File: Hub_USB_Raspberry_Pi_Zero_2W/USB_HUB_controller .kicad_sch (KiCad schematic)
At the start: 1 part, among them U3 CH334F

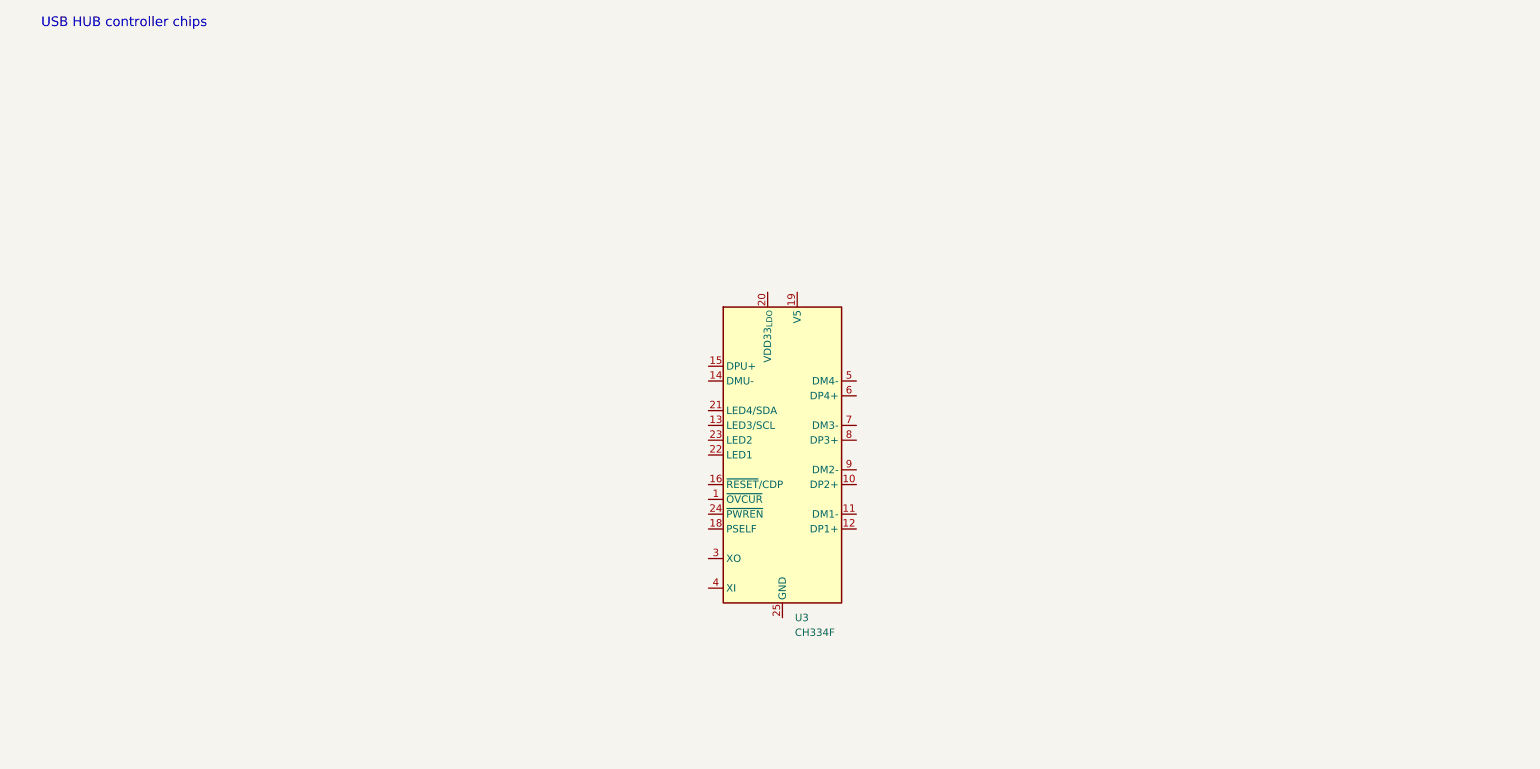
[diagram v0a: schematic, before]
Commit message: Update kicad HUB
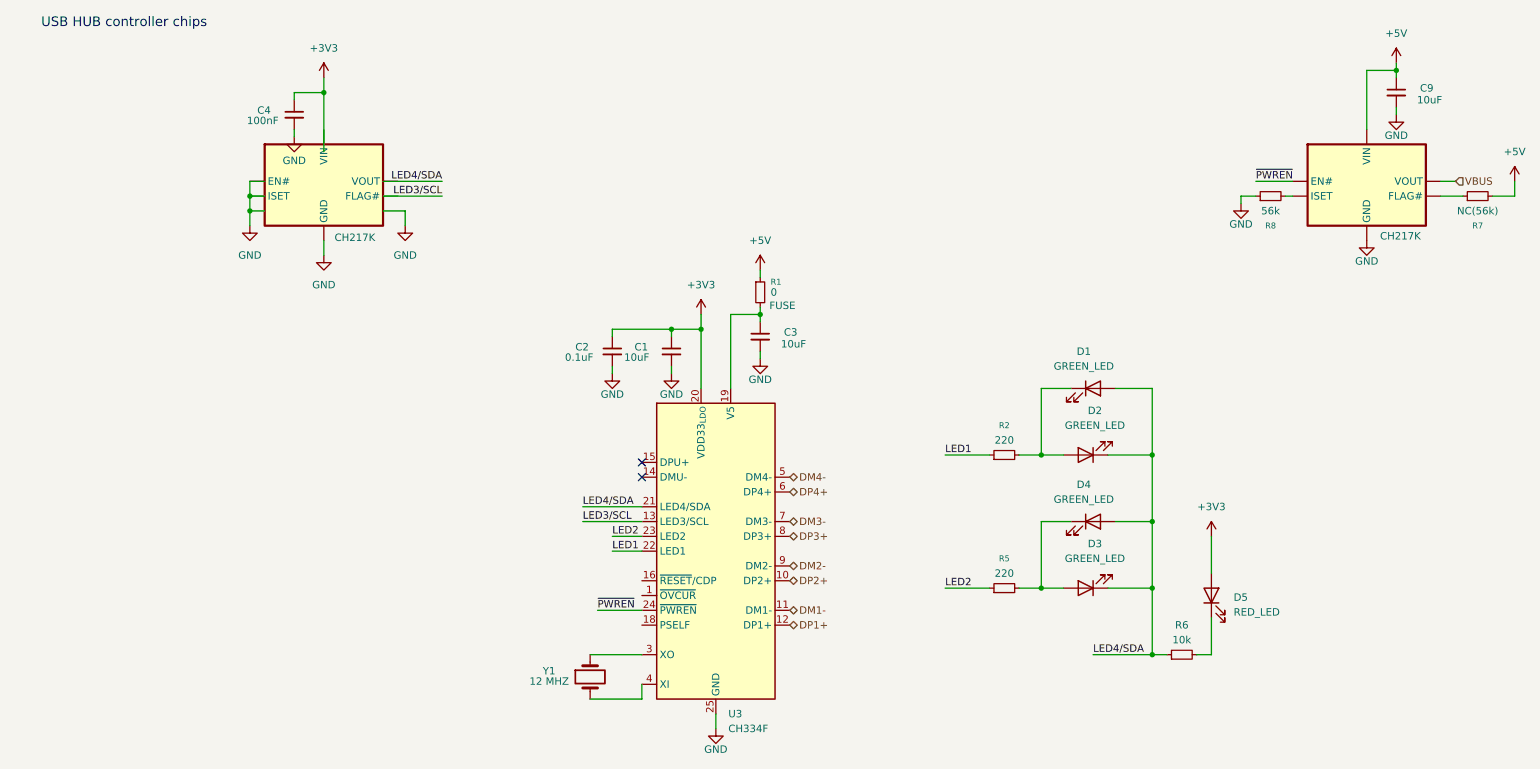
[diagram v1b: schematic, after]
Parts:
- added C1, C3, C9: 10uF, Capacitor_SMD:C_0603_1608Metric, symbol Device:C_Small
- added C2: 0.1uF, Capacitor_SMD:C_0603_1608Metric, symbol Device:C_Small
- added C4: 100nF, Capacitor_SMD:C_0603_1608Metric, symbol Device:C_Small
- added CH217K: ~, symbol Memory_EEPROM:24C02Cx-x-SN
- added CH217K1: CH217K, symbol Mylibrary:CH217K
- added D1, D2, D3, D4: GREEN_LED, LED_SMD:LED_0603_1608Metric, symbol Device:LED
- added D5: RED_LED, LED_SMD:LED_0603_1608Metric, symbol Device:LED
- added R1: 0, Fuse:Fuse_0805_2012Metric, symbol Device:R_Small
- added R2, R5: 220, symbol Device:R_Small
- added R6: 10k, Resistor_SMD:R_0603_1608Metric, symbol Device:R_Small
- added R7: NC(56k), symbol Device:R_Small
- added R8: 56k, symbol Device:R_Small
- added Y1: 12 MHZ, symbol Device:Crystal
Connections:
- net DP2+: now reaches U3.10 (DP2+)
- net DM1-: now reaches U3.11 (DM1-)
- net DP1+: now reaches U3.12 (DP1+)
- net LED3/SCL: now reaches U3.13 (LED3/SCL)
- net at U3.19 (V5): now also C3.1, R1.2
- net +3V3: now reaches U3.20 (VDD33_{LDO})
- net +3V3: now also C1.1, C2.1, C4.1, D5.2 (A)
- net LED4/SDA: now reaches U3.21 (LED4/SDA)
- net LED4/SDA: now also D1.2 (A), D2.1 (K), D3.1 (K), D4.2 (A), R6.1
- net LED1: now reaches U3.22 (LED1)
- net LED1: now also R2.1
- net LED2: now reaches U3.23 (LED2)
- net LED2: now also R5.1
- net ~{PWREN}: now reaches U3.24 (~{PWREN})
- net ~{PWREN}: now also CH217K1. (FLAG#)
- net GND: now reaches U3.25 (GND)
- net GND: now also C1.2, C2.2, C3.2, C4.2, C9.2, CH217K. (FLAG#), CH217K1. (FLAG#), R8.1
- net at U3.3 (XO): now also Y1.1
- net at U3.4 (XI): now also Y1.2
- net DM4-: now reaches U3.5 (DM4-)
- net DP4+: now reaches U3.6 (DP4+)
- net DM3-: now reaches U3.7 (DM3-)
- net DP3+: now reaches U3.8 (DP3+)
- net DM2-: now reaches U3.9 (DM2-)
- new net: D5.1 (K), R6.2
- new net: D1.1 (K), D2.2 (A), R2.2
- new net: D3.2 (A), D4.1 (K), R5.2
- new net: CH217K1. (FLAG#), R8.2
- new net: CH217K1. (FLAG#), R7.1
- new net +5V: C9.1, CH217K1. (FLAG#), R1.1, R7.2
- new net VBUS: CH217K1. (FLAG#)
- no-connect marks 0 -> 2
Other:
- moved on the sheet: U3

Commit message: CB avançage
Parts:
- removed CH217K: ~, symbol Memory_EEPROM:24C02Cx-x-SN
- added C101: 470uF, Capacitor_SMD:CP_Elec_10x10.5, symbol Device:C_Polarized
- added C11: 1uF, Capacitor_SMD:C_0603_1608Metric, symbol Device:C_Small
- added R9: NC(4k7), Resistor_SMD:R_0805_2012Metric, symbol Device:R_Small
- added TP5: Data -, TestPoint:TestPoint_Pad_D1.0mm, symbol Connector:TestPoint
- added TP6: Data +, TestPoint:TestPoint_Pad_D1.0mm, symbol Connector:TestPoint
- added TP7: Alim, TestPoint:TestPoint_Pad_D1.5mm, symbol Connector:TestPoint
- added TP8: Masse, TestPoint:TestPoint_Pad_D1.5mm, symbol Connector:TestPoint
- added U5: 24C02Cx-x-SN, Package_SO:SOIC-8_3.9x4.9mm_P1.27mm, symbol Memory_EEPROM:24C02Cx-x-SN
- CH217K1: footprint (none) -> MaximeRempreinte:CH217DS1; MPN (none) -> C7462749
- R2, R5: footprint (none) -> Resistor_SMD:R_0603_1608Metric
- R7, R8: footprint (none) -> Resistor_SMD:R_0805_2012Metric
- U6: renamed from U3; MPN (none) -> C5187527
- Y1: footprint (none) -> Crystal:Crystal_SMD_5032-4Pin_5.0x3.2mm
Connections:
- net +3V3: now also R9.1, U5.8 (VCC)
- net +5V: now also CH217K1.1 (VIN), C101.1, C11.1, TP7.1; no longer CH217K1. (FLAG#)
- net GND: now also CH217K1.2 (GND), C101.2, C11.2, TP8.1, U5.1 (A0), U5.2 (A1), U5.3 (A2), U5.4 (GND), U5.7 (WP); no longer CH217K1. (FLAG#)
- net LED3/SCL: now also U5.6 (SCL)
- net LED4/SDA: now also U5.5 (SDA)
- net VBUS: now also CH217K1.6 (VOUT); no longer CH217K1. (FLAG#)
- net ~{PWREN}: now also CH217K1.3 (EN#); no longer CH217K1. (FLAG#)
- net OVCUR#: now reaches U6.1 (~{OVCUR})
- net OVCUR#: now also CH217K1.4 (FLAG#), R7.1
- net at U6.14 (DMU-): now also TP5.1
- net at U6.15 (DPU+): now also TP6.1
- net at U6.16 (~{RESET}/CDP): now also R9.2
- net at R8.2: now also CH217K1.5 (ISET); no longer CH217K1. (FLAG#)
- no-connect marks 2 -> 1
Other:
- moved on the sheet: C3, C4, C9, D1, D2, D3, D4, D5, R1, R2, R5, R6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
